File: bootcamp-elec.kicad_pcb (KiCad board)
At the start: 2 copper layers, 28.9 x 36.4 mm, 19 parts, among them J3 FTDI, SW1 SW_Push, U1 ATmega328P-A, Y1 16MHz

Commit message: resolve DRC errors/warns
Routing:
- net GND: track 0.00 -> 8.66 mm, vias 0 -> 5
- net Net-(C4-Pad1): track 2.38 -> 6.88 mm
- net RXI: track 27.5 -> 28.3 mm
- net DTR: track 83.9 -> 83.2 mm

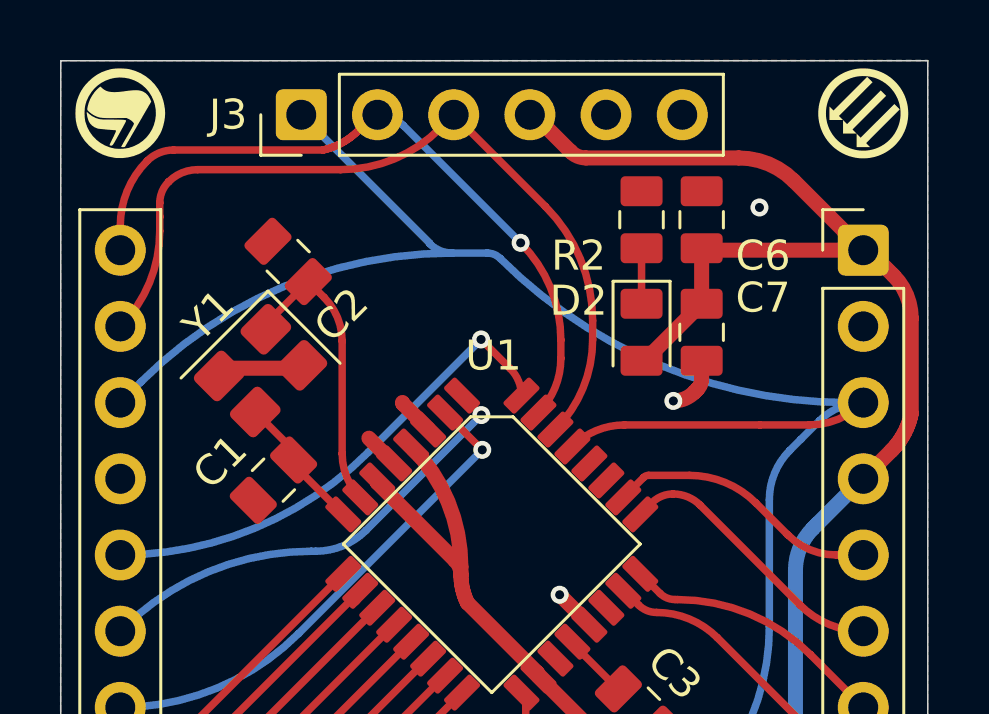
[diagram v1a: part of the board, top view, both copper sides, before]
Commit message: add tear drops
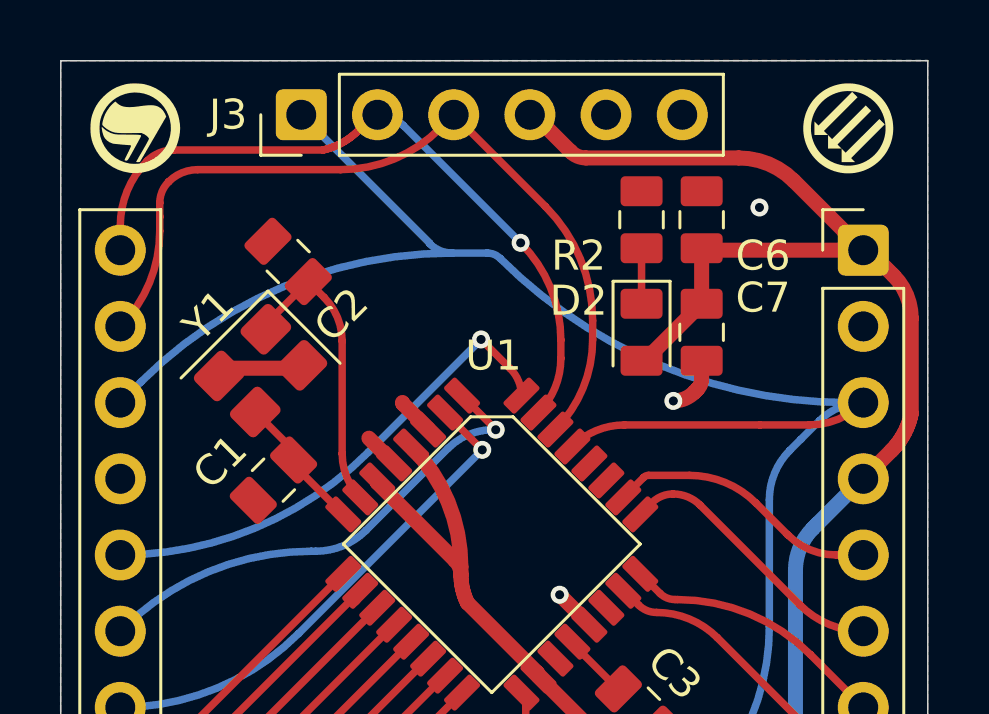
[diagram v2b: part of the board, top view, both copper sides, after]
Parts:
- moved G*** 0.71 mm to (227.8, 104.5)
- moved G*** 0.71 mm to (204.1, 104.4)
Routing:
- net D3: track 15.4 -> 16.3 mm

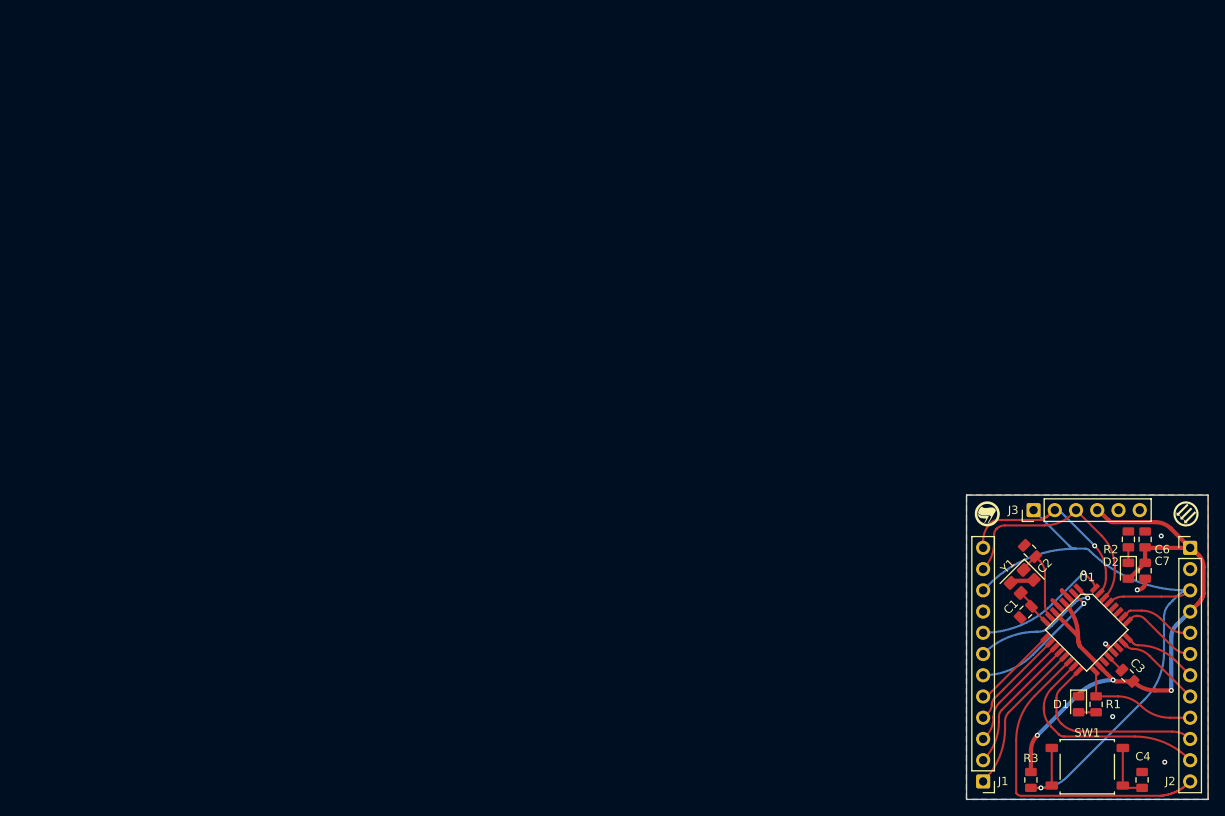
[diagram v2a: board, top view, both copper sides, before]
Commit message: add Drill/Place File Origin
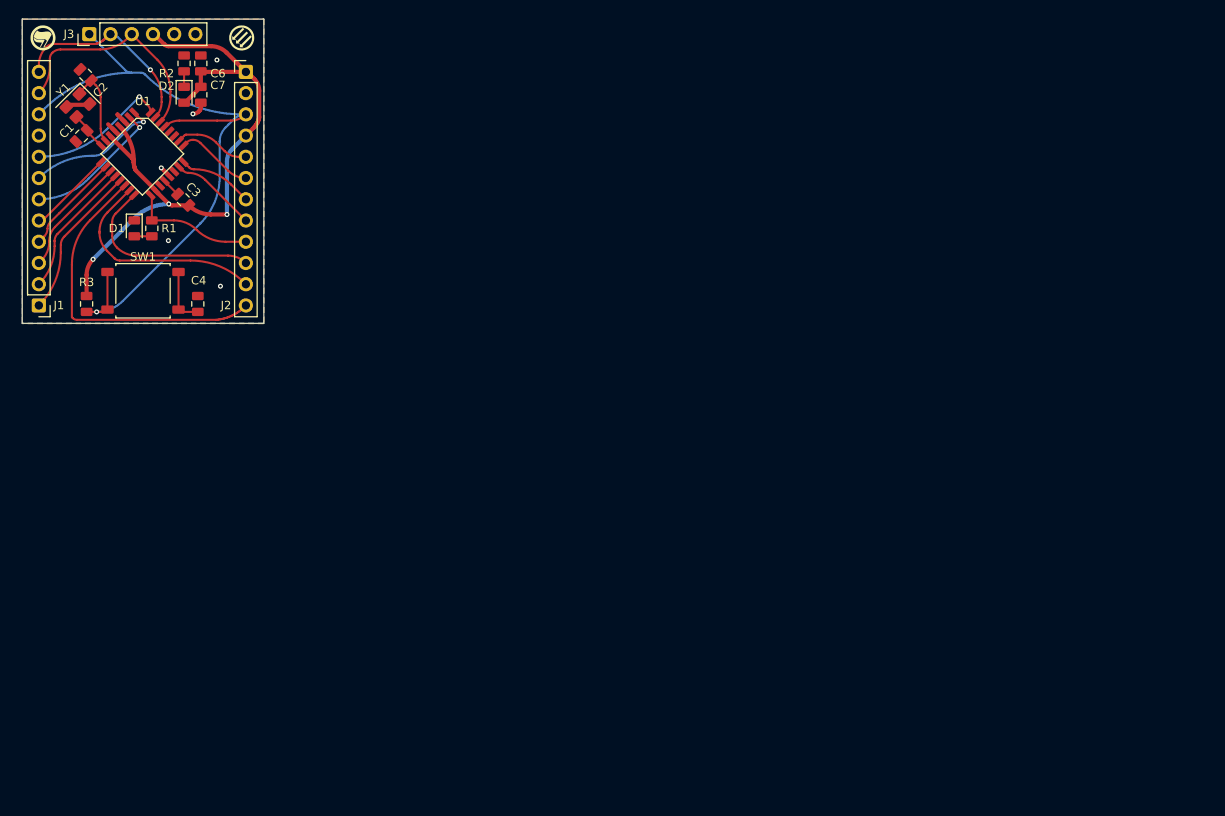
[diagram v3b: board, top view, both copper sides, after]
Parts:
- moved C2 126.5 mm to (96.2, 52.0)
- moved C3 126.5 mm to (107.9, 66.9)
- moved C4 126.5 mm to (109.6, 79.3)
- moved D2 126.5 mm to (108.0, 54.3)
- moved G*** 126.5 mm to (91.1, 47.5)
- moved J1 126.5 mm to (90.6, 79.5)
- moved R2 126.5 mm to (108.0, 50.6)
- moved R3 126.5 mm to (96.3, 79.3)
- moved U1 126.5 mm to (103.0, 61.4)
- moved C1 126.5 mm to (95.7, 59.2)
- moved C6 126.5 mm to (110.0, 50.6)
- moved C7 126.5 mm to (110.0, 54.3)
- moved D1 126.5 mm to (102.0, 70.3)
- moved G*** 126.5 mm to (114.9, 47.5)
- moved J2 126.5 mm to (115.4, 51.6)
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
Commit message: redesign pcb
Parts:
- removed G***: LOGO, bootcamp-elec:arrows-silkscreen
- removed G***: LOGO, bootcamp-elec:flags-silkscreen
- moved C4 29.1 mm to (106.5, 50.4), turned to -90 degrees
- moved R3 29.0 mm to (93.9, 50.4), turned to -90 degrees
- moved R2 27.9 mm to (94.1, 74.8), turned to -90 degrees
- moved SW1 25.9 mm to (100.2, 52.0)
- moved D2 23.6 mm to (96.2, 74.8)
- moved C6 12.1 mm to (99.5, 56.7), turned to 180 degrees
- moved C7 11.3 mm to (99.5, 58.6), turned to 0 degrees
- moved J2 7.78 mm to (109.1, 47.0)
- moved C2 5.80 mm to (96.4, 57.8), turned to 90 degrees
- moved U1 5.62 mm to (99.5, 65.8)
- moved C3 5.55 mm to (104.1, 71.0)
- moved Y1 4.80 mm to (93.7, 60.1), turned to 90 degrees
- moved J1 4.62 mm to (90.0, 74.9)
- moved D1 3.51 mm to (101.3, 73.7), turned to -45 degrees
- moved J3 3.43 mm to (93.2, 47.0)
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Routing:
- net DTR: track 83.2 -> 36.4 mm, vias 1 -> 2
- net D10: track 39.4 -> 17.1 mm
- net RAW: track 80.6 -> 70.1 mm, vias 3 -> 8
- net MOSI: track 26.6 -> 16.5 mm
- net D9: track 18.4 -> 9.19 mm
- net D8: track 16.3 -> 7.64 mm
- net D4: track 17.0 -> 9.00 mm
- net D7: track 14.2 -> 6.32 mm
- net D3: track 16.3 -> 8.89 mm
- net MISO: track 23.3 -> 16.1 mm
- net D6: track 12.6 -> 5.57 mm
- net D2: track 16.8 -> 11.8 mm
- net SCK: track 14.9 -> 10.5 mm
- net D5: track 10.3 -> 6.08 mm
- net Net-(U1-XTAL2/PB7): track 5.09 -> 9.26 mm
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- added copper zone on F.Cu, net RAW
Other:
- board size 28.9 x 36.4 mm -> 23.1 x 32 mm

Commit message: pcb design v3
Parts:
- added G***: LOGO, bootcamp-elec:arrows-silkscreen, F.Cu at (94.6, 74.7)
- moved R2 20.2 mm to (106.3, 58.6), turned to 90 degrees
- moved D2 18.1 mm to (104.3, 58.6), turned to 90 degrees
- moved C1 10.5 mm to (93.3, 67.5), turned to 180 degrees
- moved C2 4.78 mm to (93.3, 61.4), turned to 0 degrees
- moved Y1 4.39 mm to (93.3, 64.5), turned to -90 degrees
- moved R3 3.10 mm to (93.9, 53.5), turned to 90 degrees
- moved C6 2.57 mm to (97.0, 56.4), turned to 0 degrees
- moved C7 2.57 mm to (97.0, 58.3), turned to 180 degrees
- moved R1 2.44 mm to (102.0, 74.7), turned to -90 degrees
- moved D1 2.35 mm to (99.2, 74.7), turned to 90 degrees
- moved U1 1.46 mm to (101.0, 65.8)
- moved C3 1.46 mm to (105.6, 71.0)
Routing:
- net RAW: track 70.1 -> 50.5 mm, vias 8 -> 7
- net SCK: track 10.5 -> 15.9 mm, vias 0 -> 2
- net DTR: track 36.4 -> 41.6 mm, vias 2 -> 3
- net D5: track 6.08 -> 11.1 mm
- net Net-(U1-XTAL2/PB7): track 9.26 -> 4.37 mm
- net MISO: track 16.1 -> 12.0 mm
- net D6: track 5.57 -> 9.41 mm
- net MOSI: track 16.5 -> 13.5 mm
- net D7: track 6.32 -> 8.62 mm
- net D2: track 11.8 -> 13.8 mm, vias 1 -> 0
- net D4: track 9.00 -> 10.5 mm, vias 1 -> 0
- net A1: track 6.48 -> 4.97 mm
- net GND: track 8.81 -> 7.39 mm
- net D9: track 9.19 -> 10.5 mm
- net D8: track 7.64 -> 8.93 mm
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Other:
- outline, holes or cut-outs redrawn
